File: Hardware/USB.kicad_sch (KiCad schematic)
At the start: 0 parts

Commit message: Checkpoint
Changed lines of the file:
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@@
 (kicad_sch (version 20230121) (generator eeschema)
   (paper "A4")
-  (bus (pts (xy 241.3 25.4) (xy 266.7 25.4))
-    (stroke (width 0) (type default))
-  )
-  (label "ULPI_D[0..7]" (at 241.3 25.4 0) (fields_autoplaced)
-    (effects (font (size 1.27 1.27)) (justify left bottom))
-  )
-  (hierarchical_label "ULPI_DIR" (shape output) (at 83.82 63.5 0) (fields_autoplaced)
+  (hierarchical_label "VBUS" (shape output) (at 127 81.28 0) (fields_autoplaced)
     (effects (font (size 1.27 1.27)) (justify left))
   )
-  (hierarchical_label "ULPI_D[0..7]" (shape bidirectional) (at 266.7 25.4 0) (fields_autoplaced)
+  (hierarchical_label "D-" (shape bidirectional) (at 127 78.74 0) (fields_autoplaced)
     (effects (font (size 1.27 1.27)) (justify left))
   )
-  (hierarchical_label "ULPI_STP" (shape input) (at 83.82 66.04 0) (fields_autoplaced)
+  (hierarchical_label "D+" (shape bidirectional) (at 127 76.2 0) (fields_autoplaced)
     (effects (font (size 1.27 1.27)) (justify left))
   )
-  (hierarchical_label "VDD" (shape passive) (at 83.82 76.2 0) (fields_autoplaced)
-    (effects (font (size 1.27 1.27)) (justify left))
-  )
-  (hierarchical_label "ULPI_NXT" (shape output) (at 83.82 68.58 0) (fields_autoplaced)
-    (effects (font (size 1.27 1.27)) (justify left))
-  )
-  (hierarchical_label "RESET" (shape input) (at 83.82 71.12 0) (fields_autoplaced)
-    (effects (font (size 1.27 1.27)) (justify left))
-  )
-  (hierarchical_label "ULPI_CK" (shape output) (at 83.82 60.96 0) (fields_autoplaced)
-    (effects (font (size 1.27 1.27)) (justify left))
-  )

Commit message: Checkpoint
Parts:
- added C3: 100nF, Capacitor_SMD:C_0805_2012Metric, symbol Device:C
- added J1: USB_C_Receptacle_USB2.0, leptunKicadLib:USB4110-GF-A, symbol Connector:USB_C_Receptacle_USB2.0
- added R1: 330R, Resistor_SMD:R_0805_2012Metric, symbol Device:R
- added R44, R45: 5.1K, symbol Device:R_Small
- added U10: USBLC6-2SC6, Package_TO_SOT_SMD:SOT-23-6, symbol Power_Protection:USBLC6-2SC6
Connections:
- net D+: now also U10.3 (I/O2)
- net D-: now also U10.4 (I/O2)
- net VBUS: now also J1.A4 (VBUS), J1.A9 (VBUS), J1.B4 (VBUS), J1.B9 (VBUS), U10.5 (VBUS)
- new net: J1.B5 (CC2), R45.2
- new net: C3.2, J1.S1 (SHIELD), R1.2
- new net: J1.A5 (CC1), R44.2
- new net: J1.A6 (D+), J1.B6 (D+), U10.1 (I/O1)
- new net: J1.A7 (D-), J1.B7 (D-), U10.6 (I/O1)
- new net GND: C3.1, J1.A1 (GND), J1.A12 (GND), J1.B1 (GND), J1.B12 (GND), R1.1, R44.1, R45.1, U10.2 (GND)
- no-connect marks 0 -> 2

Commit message: Checkpoint
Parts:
- added TP8: ~, symbol Connector:TestPoint
- C3: footprint Capacitor_SMD:C_0805_2012Metric -> (none)
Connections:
- new net SOF: TP8.1
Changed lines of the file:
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@@
     (stroke (width 0) (type default))
+  )
+  (hierarchical_label "SOF" (shape input) (at 266.7 20.32 0) (fields_autoplaced)
+    (effects (font (size 1.27 1.27)) (justify left))
   )
   (hierarchical_label "VBUS" (shape output) (at 172.72 76.2 0) (fields_autoplaced)
@@
       (effects (font (size 1.27 1.27)))
     )
-    (property "Footprint" "Capacitor_SMD:C_0805_2012Metric" (at 121.92 122.8852 0)
+    (property "Footprint" "" (at 121.92 122.8852 0)
       (effects (font (size 1.27 1.27)) hide)
     )
@@
         )
       )
+    )
+  )
+  (symbol (lib_id "Connector:TestPoint") (at 266.7 20.32 90) (unit 1)
+    (in_bom yes) (on_board yes) (dnp no) (fields_autoplaced)
+    (property "Reference" "TP8" (at 263.398 17.78 90)
+      (effects (font (size 1.27 1.27)))
+    )
+    (property "Value" "~" (at 263.398 17.78 90)
+      (effects (font (size 1.27 1.27)) hide)
+    )
+    (property "Footprint" "" (at 266.7 15.24 0)
+      (effects (font (size 1.27 1.27)) hide)
+    )
+    (property "Datasheet" "~" (at 266.7 15.24 0)
+      (effects (font (size 1.27 1.27)) hide)
+    )
+    (pin "1")
+    (instances
+      (project "Avionus_Flight_Controller"
+        (path "/ddc7e940-0588-4587-8902-8ced9e615ace/d19046d9-5fb5-41f1-9a98-30f2d85e54f8"
+          (reference "TP8") (unit 1)
+        )
+      )

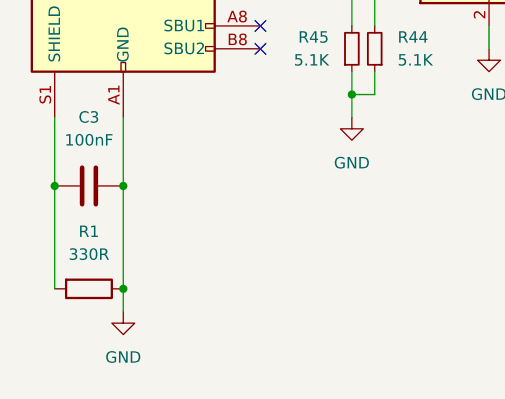
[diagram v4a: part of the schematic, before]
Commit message: ERC fixes
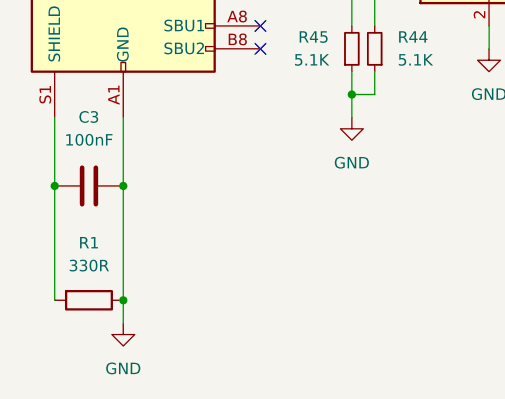
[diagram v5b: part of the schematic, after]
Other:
- moved on the sheet: R1
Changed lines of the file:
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@@
 (kicad_sch (version 20230121) (generator eeschema)
   (paper "A4")
-  (junction (at 129.54 133.35) (diameter 0) (color 0 0 0 0)
-  )
   (junction (at 147.32 96.52) (diameter 0) (color 0 0 0 0)
   )
@@
   )
   (junction (at 147.32 91.44) (diameter 0) (color 0 0 0 0)
+  )
+  (junction (at 129.54 134.62) (diameter 0) (color 0 0 0 0)
   )
   (junction (at 129.54 121.92) (diameter 0) (color 0 0 0 0)
@@
     (stroke (width 0) (type default))
   )
+  (wire (pts (xy 121.92 121.92) (xy 121.92 134.62))
+    (stroke (width 0) (type default))
+  )
   (wire (pts (xy 157.48 109.22) (xy 157.48 111.76))
     (stroke (width 0) (type default))
@@
     (stroke (width 0) (type default))
   )
-  (wire (pts (xy 129.54 133.35) (xy 129.54 135.89))
+  (wire (pts (xy 129.54 121.92) (xy 129.54 134.62))
     (stroke (width 0) (type default))
   )
@@
     (stroke (width 0) (type default))
   )
+  (wire (pts (xy 129.54 134.62) (xy 129.54 137.16))
+    (stroke (width 0) (type default))
+  )
   (wire (pts (xy 144.78 76.2) (xy 170.18 76.2))
     (stroke (width 0) (type default))
   )
   (wire (pts (xy 154.94 111.76) (xy 157.48 111.76))
-    (stroke (width 0) (type default))
-  )
-  (wire (pts (xy 129.54 121.92) (xy 129.54 133.35))
-    (stroke (width 0) (type default))
-  )
-  (wire (pts (xy 121.92 121.92) (xy 121.92 133.35))
     (stroke (width 0) (type default))
   )
@@
         (path "/ddc7e940-0588-4587-8902-8ced9e615ace/d19046d9-5fb5-41f1-9a98-30f2d85e54f8"
           (reference "C24") (unit 1)
+        )
+      )
+    )
+  )
+  (symbol (lib_id "power:GND") (at 129.54 137.16 0) (unit 1)
+    (in_bom yes) (on_board yes) (dnp no) (fields_autoplaced)
+    (property "Reference" "#PWR031" (at 129.54 143.51 0)
+      (effects (font (size 1.27 1.27)) hide)
+    )
+    (property "Value" "GND" (at 129.54 142.24 0)
+      (effects (font (size 1.27 1.27)))
+    )
+    (property "Footprint" "" (at 129.54 137.16 0)
+      (effects (font (size 1.27 1.27)) hide)
+    )
+    (property "Datasheet" "" (at 129.54 137.16 0)
+      (effects (font (size 1.27 1.27)) hide)
+    )
+    (pin "1")
+    (instances
+      (project "Avionus_Flight_Controller"
+        (path "/ddc7e940-0588-4587-8902-8ced9e615ace/d19046d9-5fb5-41f1-9a98-30f2d85e54f8"
+          (reference "#PWR031") (unit 1)
         )
       )
@@
     )
   )
-  (symbol (lib_id "Device:R") (at 125.73 133.35 270) (unit 1)
-    (in_bom yes) (on_board yes) (dnp no) (fields_autoplaced)
-    (property "Reference" "R1" (at 125.73 127 90)
-      (effects (font (size 1.27 1.27)))
-    )
-    (property "Value" "330R" (at 125.73 129.54 90)
-      (effects (font (size 1.27 1.27)))
-    )
-    (property "Footprint" "Resistor_SMD:R_0805_2012Metric" (at 125.73 131.572 90)
-      (effects (font (size 1.27 1.27)) hide)
-    )
-    (property "Datasheet" "~" (at 125.73 133.35 0)
+  (symbol (lib_id "Device:R") (at 125.73 134.62 270) (unit 1)
+    (in_bom yes) (on_board yes) (dnp no) (fields_autoplaced)
+    (property "Reference" "R1" (at 125.73 128.27 90)
+      (effects (font (size 1.27 1.27)))
+    )
+    (property "Value" "330R" (at 125.73 130.81 90)
+      (effects (font (size 1.27 1.27)))
+    )
+    (property "Footprint" "Resistor_SMD:R_0805_2012Metric" (at 125.73 132.842 90)
+      (effects (font (size 1.27 1.27)) hide)
+    )
+    (property "Datasheet" "~" (at 125.73 134.62 0)
       (effects (font (size 1.27 1.27)) hide)
     )
@@
         )
       )
-    )
-  )
-  (symbol (lib_id "power:GND") (at 129.54 135.89 0) (unit 1)
-    (in_bom yes) (on_board yes) (dnp no) (fields_autoplaced)
-    (property "Reference" "#PWR03" (at 129.54 142.24 0)
-      (effects (font (size 1.27 1.27)) hide)
-    )
-    (property "Value" "GND" (at 129.54 140.97 0)
-      (effects (font (size 1.27 1.27)))
-    )
-    (property "Footprint" "" (at 129.54 135.89 0)
-      (effects (font (size 1.27 1.27)) hide)
-    )
-    (property "Datasheet" "" (at 129.54 135.89 0)
-      (effects (font (size 1.27 1.27)) hide)
-    )
-    (pin "1")
-    (instances
-      (project "MUXUS"
-        (path "/4790d15d-8fc7-4350-9ac5-2cdedd8248a8"
-          (reference "#PWR03") (unit 1)
-        )
-      )
-      (project "Avionus_Flight_Controller"
-        (path "/ddc7e940-0588-4587-8902-8ced9e615ace/d19046d9-5fb5-41f1-9a98-30f2d85e54f8"
-          (reference "#PWR031") (unit 1)
-        )
-      )
